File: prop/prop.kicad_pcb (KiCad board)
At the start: 2 copper layers, 0 parts

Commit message: updated schematic
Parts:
- added C1: 10u, Capacitor_SMD:C_0603_1608Metric, F.Cu at (240.6, 93.0)
- added C10: 10u, Capacitor_SMD:C_0603_1608Metric, F.Cu at (68.1, 95.8)
- added C11: 10u, Capacitor_SMD:C_0603_1608Metric, F.Cu at (40.4, 97.7)
- added C12: 10u, Capacitor_SMD:C_0603_1608Metric, F.Cu at (47.0, 70.6)
- added C13: 10u, Capacitor_SMD:C_0603_1608Metric, F.Cu at (85.6, 87.4)
- added C1301: 0.1u, Capacitor_SMD:C_0603_1608Metric, F.Cu at (81.5, 101.6)
- added C14: 250u, Capacitor_SMD:C_0603_1608Metric, F.Cu at (57.2, 95.8)
- added C15: 250u, Capacitor_SMD:C_0603_1608Metric, F.Cu at (57.3, 89.9)
- added C16: 250u, Capacitor_SMD:C_0603_1608Metric, F.Cu at (67.0, 71.4)
- added C17: 250u, Capacitor_SMD:C_0603_1608Metric, F.Cu at (75.4, 87.4)
- added C18: 10u, Capacitor_SMD:C_0603_1608Metric, F.Cu at (61.8, 71.4)
- added C19: 10u, Capacitor_SMD:C_0603_1608Metric, F.Cu at (56.5, 75.5)
- added C2: 0.1u, Capacitor_SMD:C_0603_1608Metric, F.Cu at (40.4, 101.5)
- added C20: 250u, Capacitor_SMD:C_0603_1608Metric, F.Cu at (61.8, 74.8)
- added C21: 10u, Capacitor_SMD:C_0603_1608Metric, F.Cu at (249.4, 99.2)
- added C22: 10u, Capacitor_SMD:C_0603_1608Metric, F.Cu at (238.8, 73.2)
- added C23: 10u, Capacitor_SMD:C_0603_1608Metric, F.Cu at (255.3, 76.0)
- added C24: 250u, Capacitor_SMD:C_0603_1608Metric, F.Cu at (216.5, 82.4)
- added C25: 250u, Capacitor_SMD:C_0603_1608Metric, F.Cu at (217.0, 89.2)
- added C26: 10u, Capacitor_SMD:C_0603_1608Metric, F.Cu at (224.0, 72.1)
- added C27: 10u, Capacitor_SMD:C_0603_1608Metric, F.Cu at (230.9, 72.1)
- added C28: 250u, Capacitor_SMD:C_0603_1608Metric, F.Cu at (224.8, 85.9)
- added C3: 0.1u, Capacitor_SMD:C_0603_1608Metric, F.Cu at (73.1, 101.6)
- added C4: 100n, Capacitor_SMD:C_0603_1608Metric, F.Cu at (157.9, 99.0)
- added C5: 100n, Capacitor_SMD:C_0603_1608Metric, F.Cu at (158.1, 89.9)
- added C6: 10u, Capacitor_SMD:C_0603_1608Metric, F.Cu at (40.6, 83.0)
- added C7: 10u, Capacitor_SMD:C_0603_1608Metric, F.Cu at (80.5, 87.4)
- added C8: 10u, Capacitor_SMD:C_0603_1608Metric, F.Cu at (56.5, 71.2)
- added C9: 10u, Capacitor_SMD:C_0603_1608Metric, F.Cu at (46.7, 101.3)
- added J1: 1984989, star-common-lib:PHOENIX_1984989, F.Cu at (46.7, 61.0)
- added J10: 1984989, star-common-lib:PHOENIX_1984989, F.Cu at (164.8, 61.3)
- added J1001: CAS_stacking, star-common-lib:CAS_physical, F.Cu at (31.1, 54.7)
- added J1001: CAS_stacking, star-common-lib:CAS_physical, F.Cu at (204.5, 54.6)
- added J1001: CAS_stacking, star-common-lib:CAS_physical, F.Cu at (116.8, 54.6)
- added J11: 1984989, star-common-lib:PHOENIX_1984989, F.Cu at (147.6, 111.4)
- added J12: 1984989, star-common-lib:PHOENIX_1984989, F.Cu at (132.3, 61.3)
- added J13: 1984989, star-common-lib:PHOENIX_1984989, F.Cu at (222.2, 62.2)
- added J14: 1984989, star-common-lib:PHOENIX_1984989, F.Cu at (223.0, 110.4)
- added J15: Anderson_Powerpole, star-common-lib:Powerpole_1336G1, F.Cu at (170.7, 77.0)
- added J16: 1984989, star-common-lib:PHOENIX_1984989, F.Cu at (238.8, 62.2)
- added J2: 1984989, star-common-lib:PHOENIX_1984989, F.Cu at (63.0, 61.1)
- added J3: 1984989, star-common-lib:PHOENIX_1984989, F.Cu at (79.1, 61.2)
- added J4: 1984989, star-common-lib:PHOENIX_1984989, F.Cu at (148.6, 61.3)
- added J5: Conn_01x02, Connector_Molex:Molex_Mini-Fit_Jr_5569-02A2_2x01_P4.20mm_Horizontal, F.Cu at (167.8, 32.0)
- added J6: 1984989, star-common-lib:PHOENIX_1984989, F.Cu at (46.9, 111.3)
- added J7: 1984989, star-common-lib:PHOENIX_1984989, F.Cu at (63.0, 111.3)
- added J8: 1984989, star-common-lib:PHOENIX_1984989, F.Cu at (79.1, 111.3)
- added J9: 1984989, star-common-lib:PHOENIX_1984989, F.Cu at (164.1, 111.4)
- added R1: 20, Resistor_SMD:R_0603_1608Metric, F.Cu at (148.1, 97.9)
- added R10: 5k, Resistor_SMD:R_0603_1608Metric, F.Cu at (57.3, 100.7)
- added R11: 5k, Resistor_SMD:R_0603_1608Metric, F.Cu at (52.2, 101.3)
- added R12: 5k, Resistor_SMD:R_0603_1608Metric, F.Cu at (41.2, 78.4)
- added R13: 5k, Resistor_SMD:R_0603_1608Metric, F.Cu at (40.8, 87.5)
- added R14: 5k, Resistor_SMD:R_0603_1608Metric, F.Cu at (74.5, 71.4)
- added R15: 5k, Resistor_SMD:R_0603_1608Metric, F.Cu at (79.1, 71.4)
- added R16: 5k, Resistor_SMD:R_0603_1608Metric, F.Cu at (62.9, 94.9)
- added R17: 5k, Resistor_SMD:R_0603_1608Metric, F.Cu at (61.5, 100.7)
- added R18: 5k, Resistor_SMD:R_0603_1608Metric, F.Cu at (230.9, 79.6)
- added R19: 5k, Resistor_SMD:R_0603_1608Metric, F.Cu at (225.4, 79.6)
- added R2: 20, Resistor_SMD:R_0603_1608Metric, F.Cu at (148.0, 90.8)
- added R20: 5k, Resistor_SMD:R_0603_1608Metric, F.Cu at (246.9, 89.6)
- added R21: 5k, Resistor_SMD:R_0603_1608Metric, F.Cu at (242.4, 98.8)
- added R22: 1.2k, Resistor_SMD:R_0603_1608Metric, F.Cu at (231.3, 85.8)
- added R23: 1.2k, Resistor_SMD:R_0603_1608Metric, F.Cu at (246.9, 76.0)
- added R24: 5k, Resistor_SMD:R_0603_1608Metric, F.Cu at (233.7, 98.9)
- added R25: 5k, Resistor_SMD:R_0603_1608Metric, F.Cu at (231.5, 92.7)
- added R26: 1.2k, Resistor_SMD:R_0603_1608Metric, F.Cu at (255.1, 83.0)
- added R3: 1.2k, Resistor_SMD:R_0603_1608Metric, F.Cu at (66.4, 100.7)
- added R4: 1.2k, Resistor_SMD:R_0603_1608Metric, F.Cu at (41.1, 93.6)
- added R5: 1.2k, Resistor_SMD:R_0603_1608Metric, F.Cu at (41.1, 70.6)
- added R6: 1.2k, Resistor_SMD:R_0603_1608Metric, F.Cu at (85.5, 71.4)
- added R7: 1.2k, Resistor_SMD:R_0603_1608Metric, F.Cu at (51.5, 70.6)
- added R8: 5k, Resistor_SMD:R_0603_1608Metric, F.Cu at (41.2, 74.7)
- added R9: 5k, Resistor_SMD:R_0603_1608Metric, F.Cu at (49.9, 90.0)
- added U10: LM386, Package_SO:SOIC-8_3.9x4.9mm_P1.27mm, F.Cu at (48.4, 76.7)
- added U11: LM386, Package_SO:SOIC-8_3.9x4.9mm_P1.27mm, F.Cu at (75.1, 79.5)
- added U12: LM386, Package_SO:SOIC-8_3.9x4.9mm_P1.27mm, F.Cu at (57.0, 82.7)
- added U13: LM386, Package_SO:SOIC-8_3.9x4.9mm_P1.27mm, F.Cu at (216.9, 74.7)
- added U1301: MAX6675ISA+, star-common-lib:SOIC127P600X175-8N, F.Cu at (74.5, 94.9)
- added U14: LM386, Package_SO:SOIC-8_3.9x4.9mm_P1.27mm, F.Cu at (255.3, 91.8)
- added U15: MCP3008, Package_SO:SOIC-16_3.9x9.9mm_P1.27mm, F.Cu at (221.4, 97.2)
- added U16: LM386, Package_SO:SOIC-8_3.9x4.9mm_P1.27mm, F.Cu at (239.5, 82.8)
- added U2: MAX6675ISA+, star-common-lib:SOIC127P600X175-8N, F.Cu at (83.8, 79.5)
- added U3: MAX6675ISA+, star-common-lib:SOIC127P600X175-8N, F.Cu at (82.8, 94.7)
- added U4: LM386, Package_SO:SOIC-8_3.9x4.9mm_P1.27mm, F.Cu at (48.4, 84.7)
- added U5: MCP3008, Package_SO:SOIC-16_3.9x9.9mm_P1.27mm, F.Cu at (65.9, 84.1)
- added U6: L298P, star-common-lib:SOIC127P1420X360-20N, F.Cu at (134.2, 94.5)
- added U7: SN74LVC8T245DBR, star-common-lib:SN74LVC8T245DBR_SOP65P780X200-24N, F.Cu at (168.0, 94.4)
- added U8: SN74LVC2GU04DCKR, star-common-lib:SN74LVC2GU04_SOT65P210X110-6N, F.Cu at (152.7, 94.4)
- added U9: LM386, Package_SO:SOIC-8_3.9x4.9mm_P1.27mm, F.Cu at (48.6, 95.1)
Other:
- board outline added: 63.5 x 63.5 mm
- rule pad_to_mask_clearance: 0.05 -> 0.051

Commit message: more updates to layout
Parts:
- removed J15: Anderson_Powerpole, star-common-lib:Powerpole_1336G1
- moved C3 79.0 mm to (146.7, 72.6), turned to 0 degrees
- moved U3 73.2 mm to (153.4, 75.5), turned to 90 degrees
- moved J5 71.3 mm to (166.2, 103.3), turned to 180 degrees
- moved C1301 52.0 mm to (39.9, 70.4), turned to 90 degrees
- moved J14 50.9 mm to (236.3, 61.2), turned to 180 degrees
- moved R4 47.1 mm to (82.3, 70.7)
- moved R11 39.8 mm to (82.3, 75.2), turned to 270 degrees
- moved C18 38.8 mm to (86.4, 101.4), turned to 270 degrees
- moved C11 38.2 mm to (72.9, 77.6), turned to 0 degrees
- moved U2 37.2 mm to (46.6, 79.2), turned to 0 degrees
- moved U1301 36.3 mm to (46.6, 71.6), turned to 0 degrees
- moved U9 35.3 mm to (75.2, 71.9)
- moved C16 34.9 mm to (49.1, 101.3), turned to 270 degrees
- moved C20 33.5 mm to (82.3, 101.4), turned to 270 degrees
- moved C19 32.9 mm to (82.3, 95.9)
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
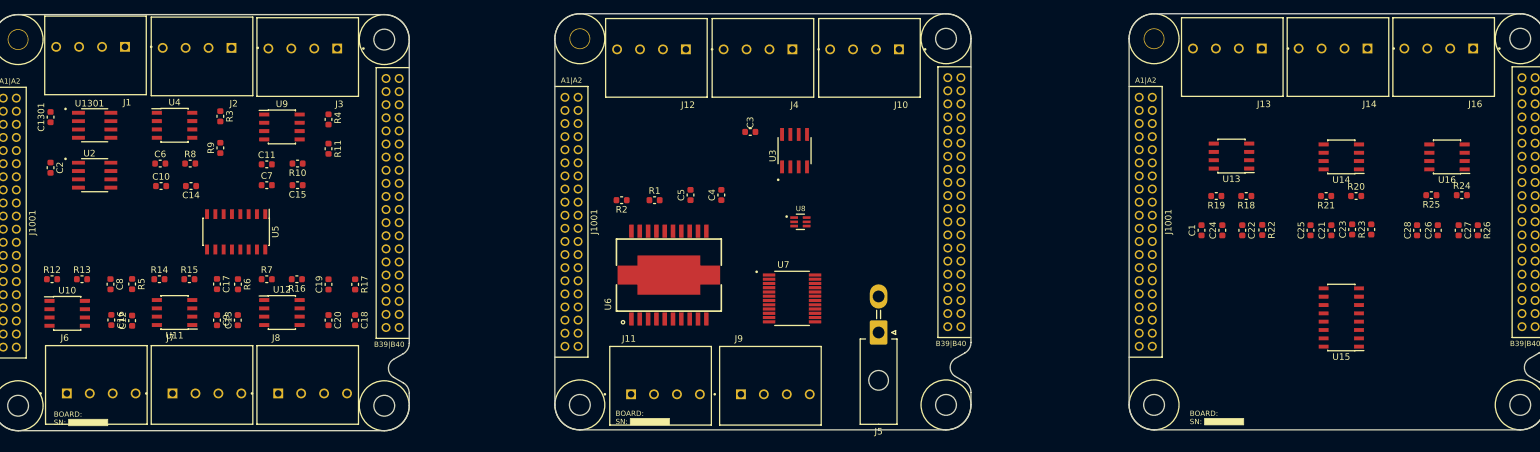
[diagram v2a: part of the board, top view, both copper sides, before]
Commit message: changed to 4 layer board
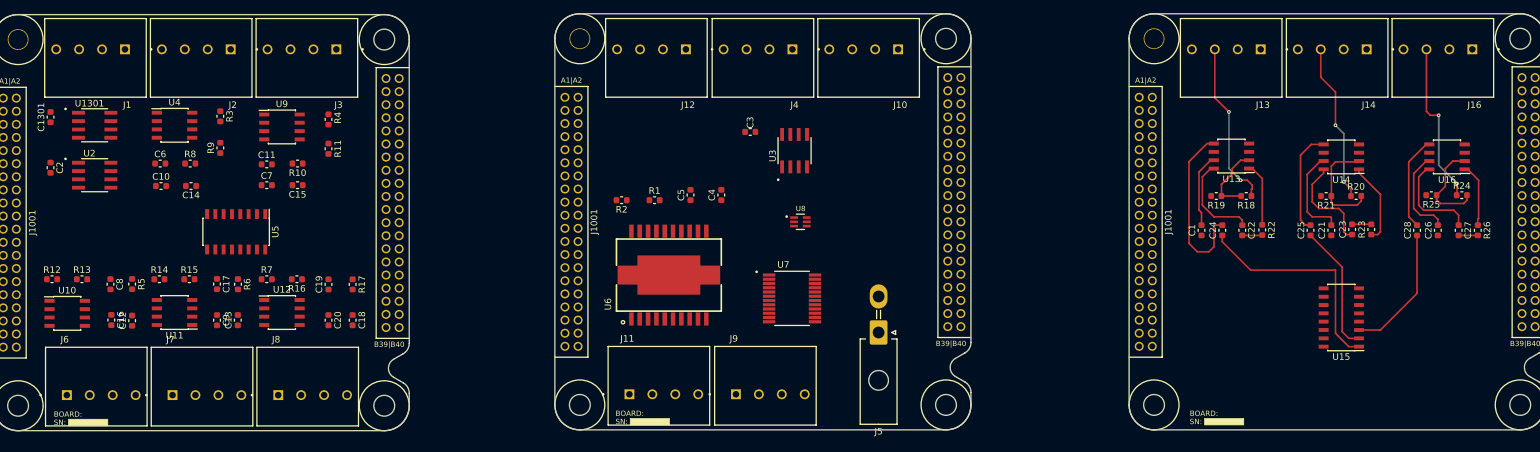
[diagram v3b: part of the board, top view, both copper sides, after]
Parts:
- moved J9 0.76 mm to (149.0, 111.4)
- moved C18 0.38 mm to (86.0, 101.4)
- moved J1 0.38 mm to (46.7, 61.3)
- moved R17 0.38 mm to (86.0, 95.9)
- moved J2 0.26 mm to (62.9, 61.3)
- moved J6 0.25 mm to (46.9, 111.5)
- moved J7 0.25 mm to (63.0, 111.5)
- moved J8 0.25 mm to (79.1, 111.5)
- moved J11 0.25 mm to (132.7, 111.4)
- moved J13 0.21 mm to (220.1, 61.3)
- moved J14 0.18 mm to (236.2, 61.3)
- moved J16 0.18 mm to (252.3, 61.3)
- moved J3 0.18 mm to (79.0, 61.3)
- moved J10 0.13 mm to (164.7, 61.3)
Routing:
- net /ADC_Amp_Extra/Data0: track 0.00 -> 34.1 mm
- net Net-(C24-Pad2): track 0.00 -> 26.5 mm
- net /ADC_Amp_Extra/aData0: track 0.00 -> 25.4 mm, vias 0 -> 2
- net /ADC_Amp_Extra/aData2: track 0.00 -> 24.9 mm, vias 0 -> 2
- net /ADC_Amp_Extra/aData1: track 0.00 -> 24.3 mm, vias 0 -> 2
- net /ADC_Amp_Extra/Data2: track 0.00 -> 20.0 mm
- net /ADC_Amp_Extra/Data1: track 0.00 -> 19.7 mm
- net Net-(C25-Pad2): track 0.00 -> 16.0 mm
- net Net-(R20-Pad2): track 0.00 -> 15.9 mm
- net Net-(C23-Pad1): track 0.00 -> 15.5 mm
- net Net-(C27-Pad1): track 0.00 -> 14.7 mm
- net Net-(R24-Pad2): track 0.00 -> 14.6 mm
- net Net-(C28-Pad2): track 0.00 -> 14.4 mm
- net Net-(C22-Pad1): track 0.00 -> 14.4 mm
- net Net-(C21-Pad2): track 0.00 -> 14.3 mm
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- added copper zone on PWR, net +5V
- added copper zone on GND, net GND
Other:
- copper layers 2 -> 4

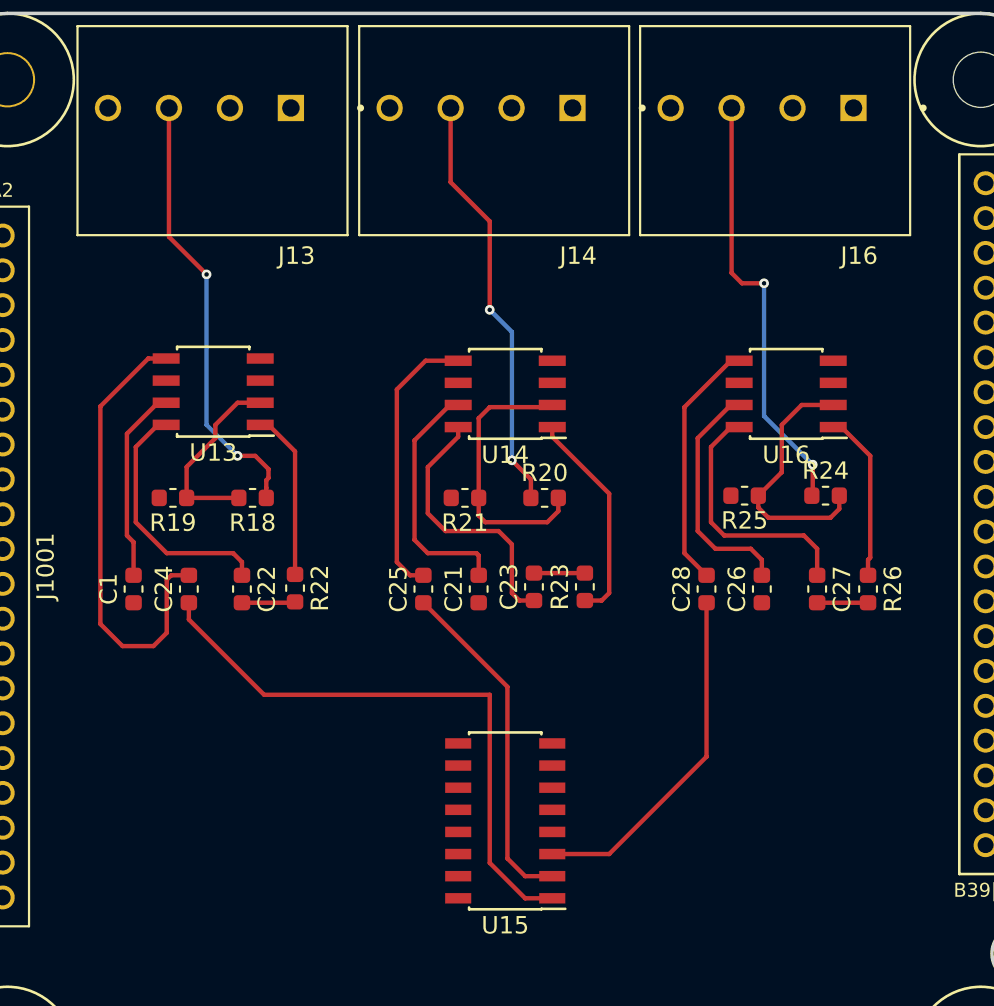
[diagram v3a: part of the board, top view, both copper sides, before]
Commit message: more layout progress on 4 layer board
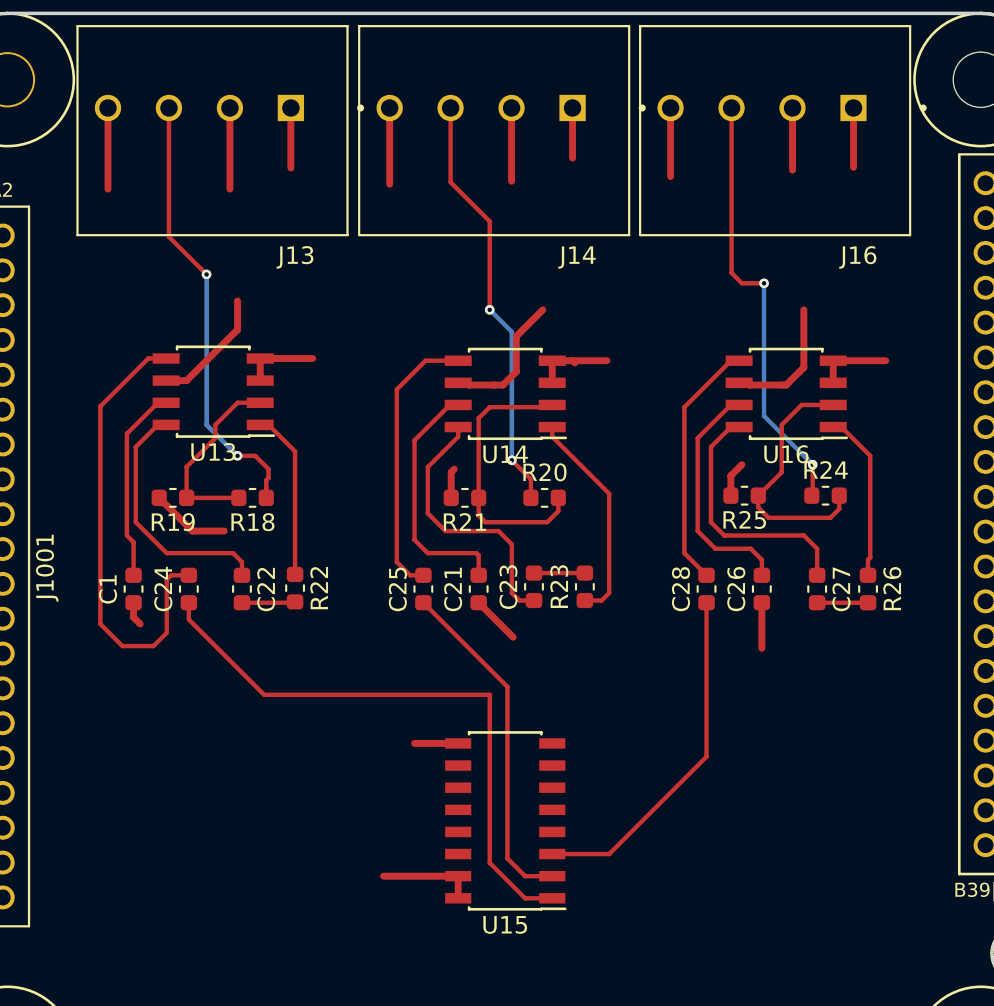
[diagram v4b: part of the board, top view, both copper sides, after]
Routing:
- net GND: track 0.00 -> 56.2 mm
- net +5V: track 0.00 -> 37.6 mm
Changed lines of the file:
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@@
     (thickness 1.6)
     (drawings 0)
-    (tracks 145)
+    (tracks 192)
     (zones 0)
     (modules 89)
@@
   )
   (setup
-    (last_trace_width 0.254)
+    (last_trace_width 0.39878)
     (user_trace_width 0.254)
+    (user_trace_width 0.39878)
     (trace_clearance 0.2)
     (zone_clearance 0.508)
@@
       (net 1 GND))
   )
+  (segment (start 214.051 60.041) (end 214.051 64.699) (width 0.39878) (layer F.Cu) (net 1))
+  (segment (start 221.051 60.041) (end 221.051 64.699) (width 0.39878) (layer F.Cu) (net 1))
+  (segment (start 230.22 60.041) (end 230.22 64.42) (width 0.39878) (layer F.Cu) (net 1))
+  (segment (start 237.22 60.041) (end 237.22 64.246) (width 0.39878) (layer F.Cu) (net 1))
+  (segment (start 246.349 60.041) (end 246.349 63.977) (width 0.39878) (layer F.Cu) (net 1))
+  (segment (start 253.349 60.041) (end 253.349 63.611) (width 0.39878) (layer F.Cu) (net 1))
+  (segment (start 239.555 74.549) (end 239.555 75.819) (width 0.39878) (layer F.Cu) (net 1))
+  (segment (start 222.791 74.422) (end 222.791 75.692) (width 0.39878) (layer F.Cu) (net 1))
+  (segment (start 255.684 74.549) (end 255.684 75.819) (width 0.39878) (layer F.Cu) (net 1))
+  (segment (start 222.791 74.422) (end 225.806 74.422) (width 0.39878) (layer F.Cu) (net 1))
+  (segment (start 240.72878 74.549) (end 240.85578 74.676) (width 0.39878) (layer F.Cu) (net 1))
+  (segment (start 239.555 74.549) (end 240.72878 74.549) (width 0.39878) (layer F.Cu) (net 1))
+  (segment (start 240.72878 74.549) (end 242.697 74.549) (width 0.39878) (layer F.Cu) (net 1))
+  (segment (start 255.684 74.549) (end 258.699 74.549) (width 0.39878) (layer F.Cu) (net 1))
+  (segment (start 251.587 88.443) (end 251.587 91.059) (width 0.39878) (layer F.Cu) (net 1))
+  (segment (start 235.331 88.443) (end 237.312 90.424) (width 0.39878) (layer F.Cu) (net 1))
+  (segment (start 215.519 88.443) (end 215.519 89.281) (width 0.39878) (layer F.Cu) (net 1))
+  (segment (start 215.519 89.281) (end 215.9 89.662) (width 0.39878) (layer F.Cu) (net 1))
+  (segment (start 233.756 82.423) (end 233.756 80.95) (width 0.39878) (layer F.Cu) (net 1))
+  (segment (start 233.756 80.95) (end 233.934 80.772) (width 0.39878) (layer F.Cu) (net 1))
+  (segment (start 218.897 84.328) (end 220.726 84.328) (width 0.39878) (layer F.Cu) (net 1))
+  (segment (start 216.992 82.423) (end 218.897 84.328) (width 0.39878) (layer F.Cu) (net 1))
+  (segment (start 249.809 82.296) (end 249.809 81.153) (width 0.39878) (layer F.Cu) (net 1))
+  (segment (start 249.809 81.153) (end 250.444 80.518) (width 0.39878) (layer F.Cu) (net 1))
+  (segment (start 234.155 96.52) (end 231.648 96.52) (width 0.39878) (layer F.Cu) (net 1))
+  (segment (start 218.56478 75.692) (end 221.488 72.76878) (width 0.39878) (layer F.Cu) (net 10))
+  (segment (start 217.391 75.692) (end 218.56478 75.692) (width 0.39878) (layer F.Cu) (net 10))
+  (segment (start 221.488 72.76878) (end 221.488 71.12) (width 0.39878) (layer F.Cu) (net 10))
+  (segment (start 234.63 75.819) (end 234.757 75.946) (width 0.39878) (layer F.Cu) (net 10))
+  (segment (start 234.155 75.819) (end 234.63 75.819) (width 0.39878) (layer F.Cu) (net 10))
+  (segment (start 234.757 75.946) (end 236.22 75.946) (width 0.39878) (layer F.Cu) (net 10))
+  (segment (start 236.22 75.946) (end 236.728 75.946) (width 0.39878) (layer F.Cu) (net 10))
+  (segment (start 236.728 75.946) (end 237.49 75.184) (width 0.39878) (layer F.Cu) (net 10))
+  (segment (start 237.49 75.184) (end 237.49 73.152) (width 0.39878) (layer F.Cu) (net 10))
+  (segment (start 237.49 73.152) (end 239.014 71.628) (width 0.39878) (layer F.Cu) (net 10))
+  (segment (start 250.759 75.819) (end 250.886 75.946) (width 0.39878) (layer F.Cu) (net 10))
+  (segment (start 250.284 75.819) (end 250.759 75.819) (width 0.39878) (layer F.Cu) (net 10))
+  (segment (start 250.886 75.946) (end 252.73 75.946) (width 0.39878) (layer F.Cu) (net 10))
+  (segment (start 252.73 75.946) (end 252.984 75.946) (width 0.39878) (layer F.Cu) (net 10))
+  (segment (start 252.984 75.946) (end 253.746 75.184) (width 0.39878) (layer F.Cu) (net 10))
+  (segment (start 253.746 75.184) (end 254 74.93) (width 0.39878) (layer F.Cu) (net 10))
+  (segment (start 254 74.93) (end 254 71.628) (width 0.39878) (layer F.Cu) (net 10))
+  (segment (start 256.849 60.041) (end 256.849 63.445) (width 0.39878) (layer F.Cu) (net 10))
+  (segment (start 240.72 60.041) (end 240.72 62.92) (width 0.39878) (layer F.Cu) (net 10))
+  (segment (start 224.551 60.041) (end 224.551 63.485) (width 0.39878) (layer F.Cu) (net 10))
+  (segment (start 234.155 105.41) (end 234.155 104.14) (width 0.39878) (layer F.Cu) (net 10))
+  (segment (start 234.155 104.14) (end 229.87 104.14) (width 0.39878) (layer F.Cu) (net 10))
   (segment (start 238.328 82.423) (end 238.328 81.356) (width 0.254) (layer F.Cu) (net 46))
   (segment (start 238.328 81.356) (end 237.236 80.264) (width 0.254) (layer F.Cu) (net 46))
@@
   (segment (start 232.283 74.549) (end 230.632 76.2) (width 0.254) (layer F.Cu) (net 138))
   (segment (start 234.155 74.549) (end 232.283 74.549) (width 0.254) (layer F.Cu) (net 138))
-  (zone (net 10) (net_name +5V) (layer PWR) (hatch edge 0.508)
+  (zone (net 1) (net_name GND) (layer GND) (hatch edge 0.508)
     (connect_pads (clearance 0.508))
     (min_thickness 0.254)
@@
     (polygon
       (pts
-        (xy 204.47 113.792) (xy 204.47 58.674) (xy 204.724 56.896) (xy 205.74 55.626) (xy 207.01 54.864)
-        (xy 208.534 54.61) (xy 210.312 54.61) (xy 263.144 54.61) (xy 265.684 54.864) (xy 266.954 55.88)
-        (xy 267.97 57.912) (xy 267.97 60.96) (xy 267.97 69.342) (xy 267.97 95.758) (xy 267.97 104.902)
-        (xy 267.208 106.426) (xy 265.176 107.442) (xy 264.922 107.95) (xy 264.922 109.22) (xy 265.684 110.236)
-        (xy 267.716 111.506) (xy 267.97 113.284) (xy 267.716 115.824) (xy 266.7 117.348) (xy 264.414 118.11)
-        (xy 260.096 118.11) (xy 250.698 118.11) (xy 231.648 118.11) (xy 208.788 118.11) (xy 206.756 117.856)
-        (xy 205.74 117.094) (xy 204.724 116.078) (xy 204.47 115.062)
+        (xy 204.47 54.61) (xy 267.97 54.61) (xy 267.97 118.11) (xy 204.47 118.11)
       )
     )
   )
-  (zone (net 1) (net_name GND) (layer GND) (hatch edge 0.508)
+  (zone (net 10) (net_name +5V) (layer PWR) (hatch edge 0.508)
     (connect_pads (clearance 0.508))
     (min_thickness 0.254)
@@
     (polygon
       (pts
-        (xy 204.47 112.776) (xy 204.47 59.182) (xy 204.978 56.388) (xy 206.756 54.864) (xy 209.804 54.61)
-        (xy 263.398 54.61) (xy 266.446 55.372) (xy 267.716 57.15) (xy 267.97 59.182) (xy 267.97 105.156)
-        (xy 267.208 106.172) (xy 265.176 107.442) (xy 264.668 108.458) (xy 265.176 109.728) (xy 267.208 111.252)
-        (xy 267.97 112.014) (xy 267.97 113.284) (xy 267.716 115.824) (xy 266.192 117.602) (xy 263.398 118.11)
-        (xy 236.728 118.11) (xy 209.804 118.11) (xy 206.756 117.856) (xy 205.232 116.586) (xy 204.47 115.316)
-        (xy 204.47 113.03)
+        (xy 204.47 54.61) (xy 267.97 54.61) (xy 267.97 118.11) (xy 204.47 118.11) (xy 204.47 54.864)
       )
     )
